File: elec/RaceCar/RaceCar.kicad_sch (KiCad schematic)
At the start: 0 parts

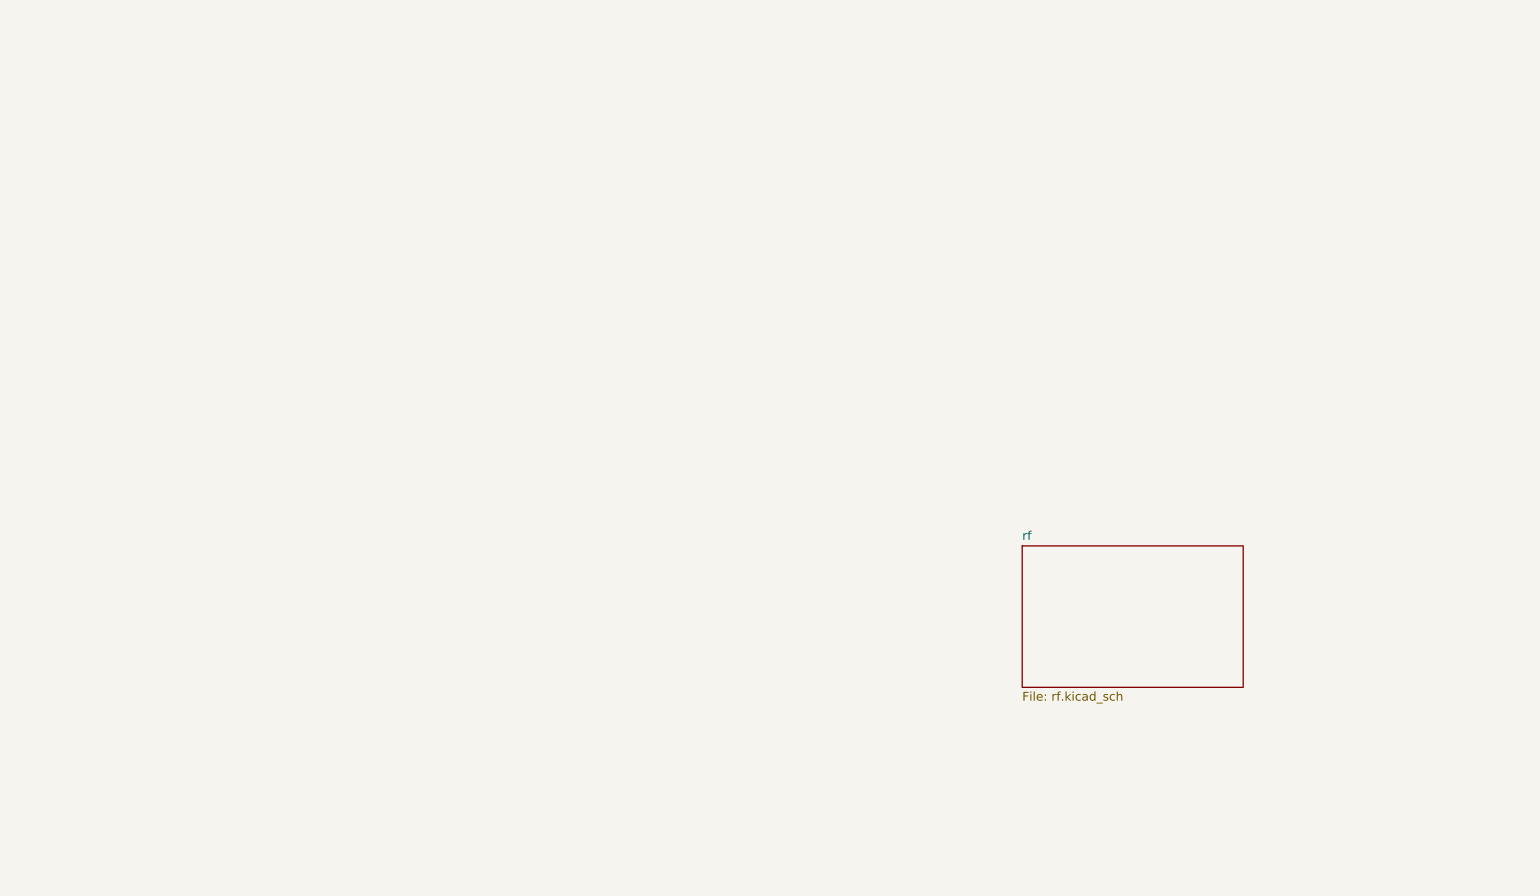
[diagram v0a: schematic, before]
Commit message: Ajout du rx
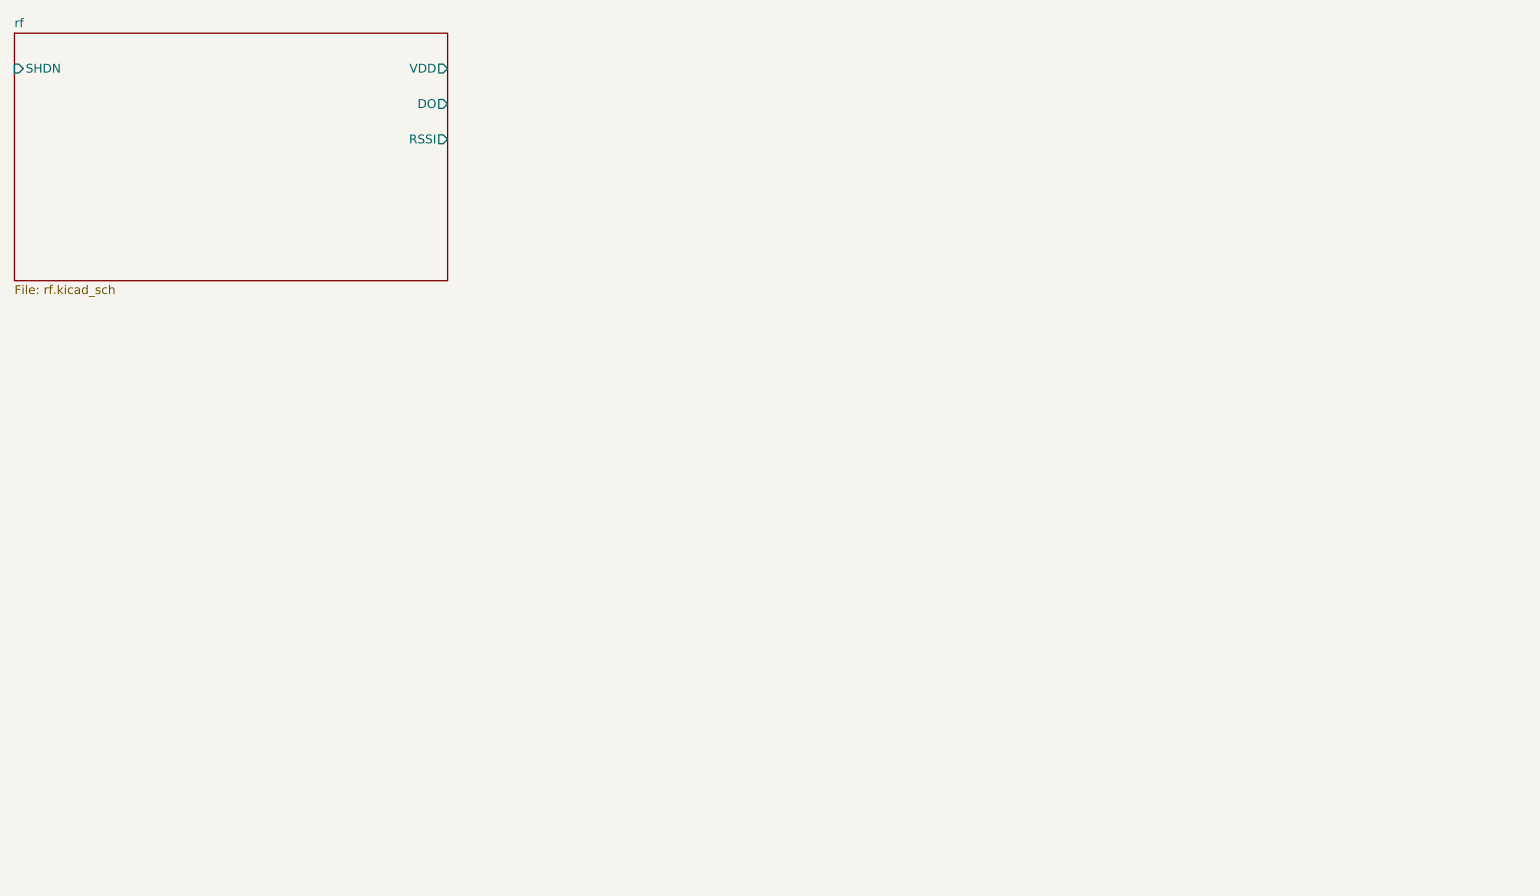
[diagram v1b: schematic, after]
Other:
- sheet rf ports: added DO, RSSI, SHDN, VDD; removed none
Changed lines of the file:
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@@
 	(generator "eeschema")
 	(generator_version "9.0")
-	(paper "A4")
+	(paper "USLetter")
 	(sheet
-		(at 168.91 104.14)
-		(size 31.75 20.32)
+		(at 24.13 30.48)
+		(size 62.23 35.56)
 		(exclude_from_sim no)
 		(in_bom yes)
@@
 		)
 		(property "Sheetname" "rf"
-			(at 168.91 103.4284 0)
+			(at 24.13 29.7684 0)
 			(effects
 				(font
@@
 		)
 		(property "Sheetfile" "rf.kicad_sch"
-			(at 168.91 125.0446 0)
+			(at 24.13 66.6246 0)
 			(effects
 				(font
@@
 			)
 		)
+		(pin "DO" output
+			(at 86.36 40.64 0)
+			(effects
+				(font
+					(size 1.27 1.27)
+				)
+				(justify right)
+			)
+		)
+		(pin "SHDN" input
+			(at 24.13 35.56 180)
+			(effects
+				(font
+					(size 1.27 1.27)
+				)
+				(justify left)
+			)
+		)
+		(pin "RSSI" output
+			(at 86.36 45.72 0)
+			(effects
+				(font
+					(size 1.27 1.27)
+				)
+				(justify right)
+			)
+		)
+		(pin "VDD" output
+			(at 86.36 35.56 0)
+			(effects
+				(font
+					(size 1.27 1.27)
+				)
+				(justify right)
+			)
+		)

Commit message: Ajout du power et du stm
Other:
- added sheet STM32 (STM32.kicad_sch)
- added sheet power (power.kicad_sch)
- sheet rf ports: added GND; removed none
